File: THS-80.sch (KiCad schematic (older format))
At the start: 19 parts, among them J1 USB_B_Micro, J2 RC80 Bus, J3 RC80 Expansion, SW1 Reset, U1 MAX40203AUK, U2 DS1813R-5+T&R

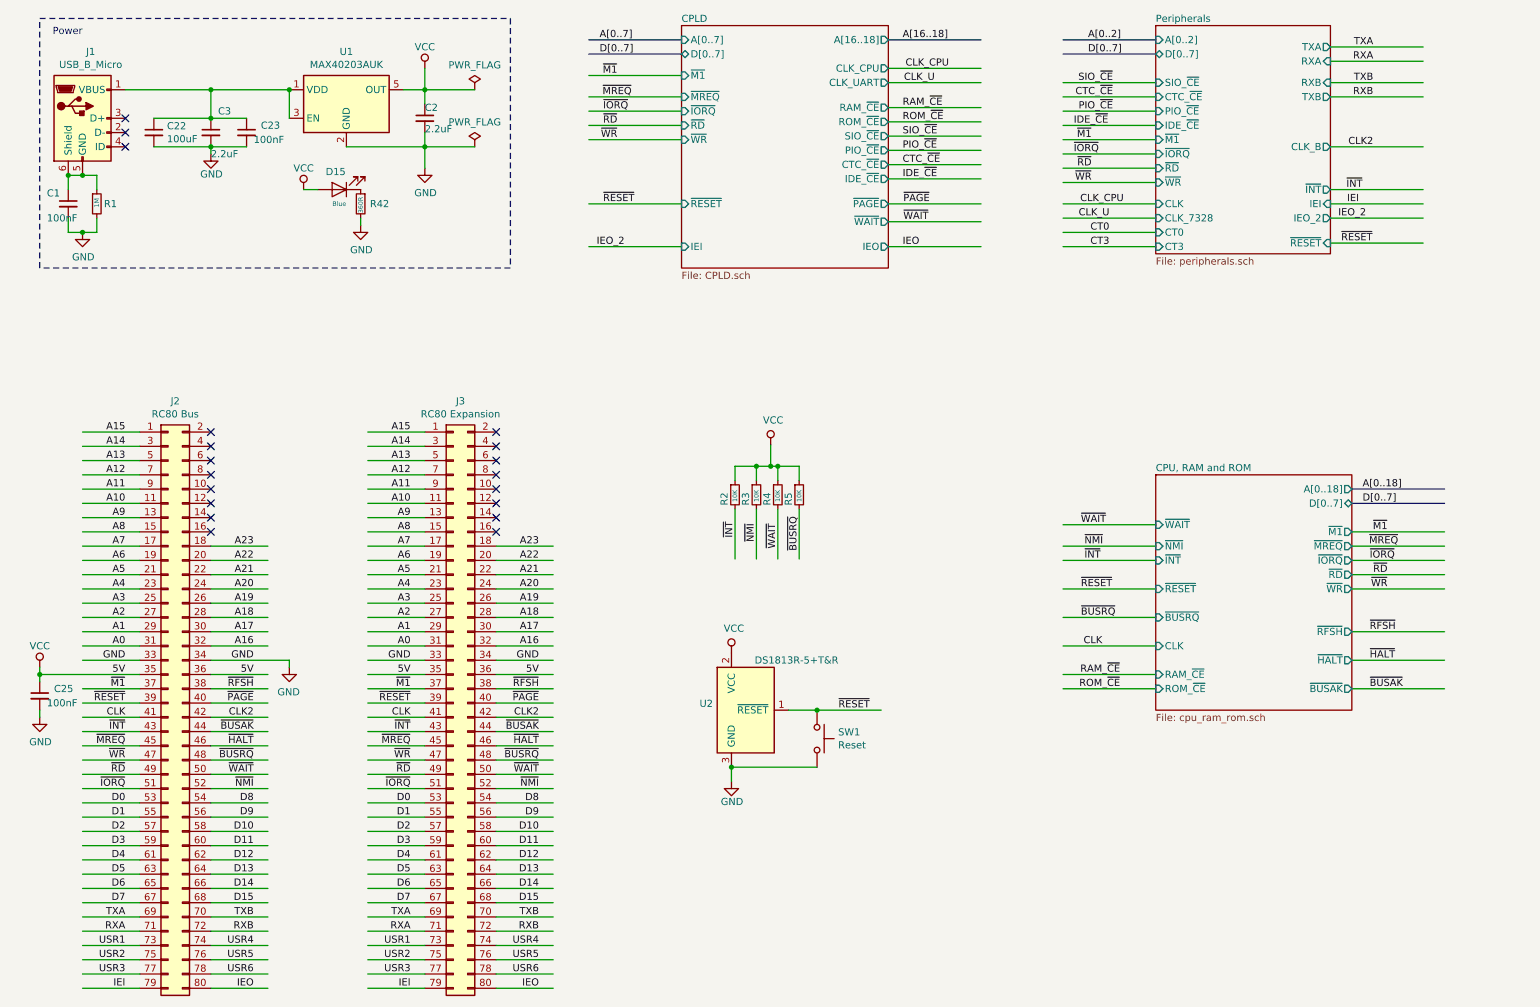
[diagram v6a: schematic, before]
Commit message: swapped CTC and PIO
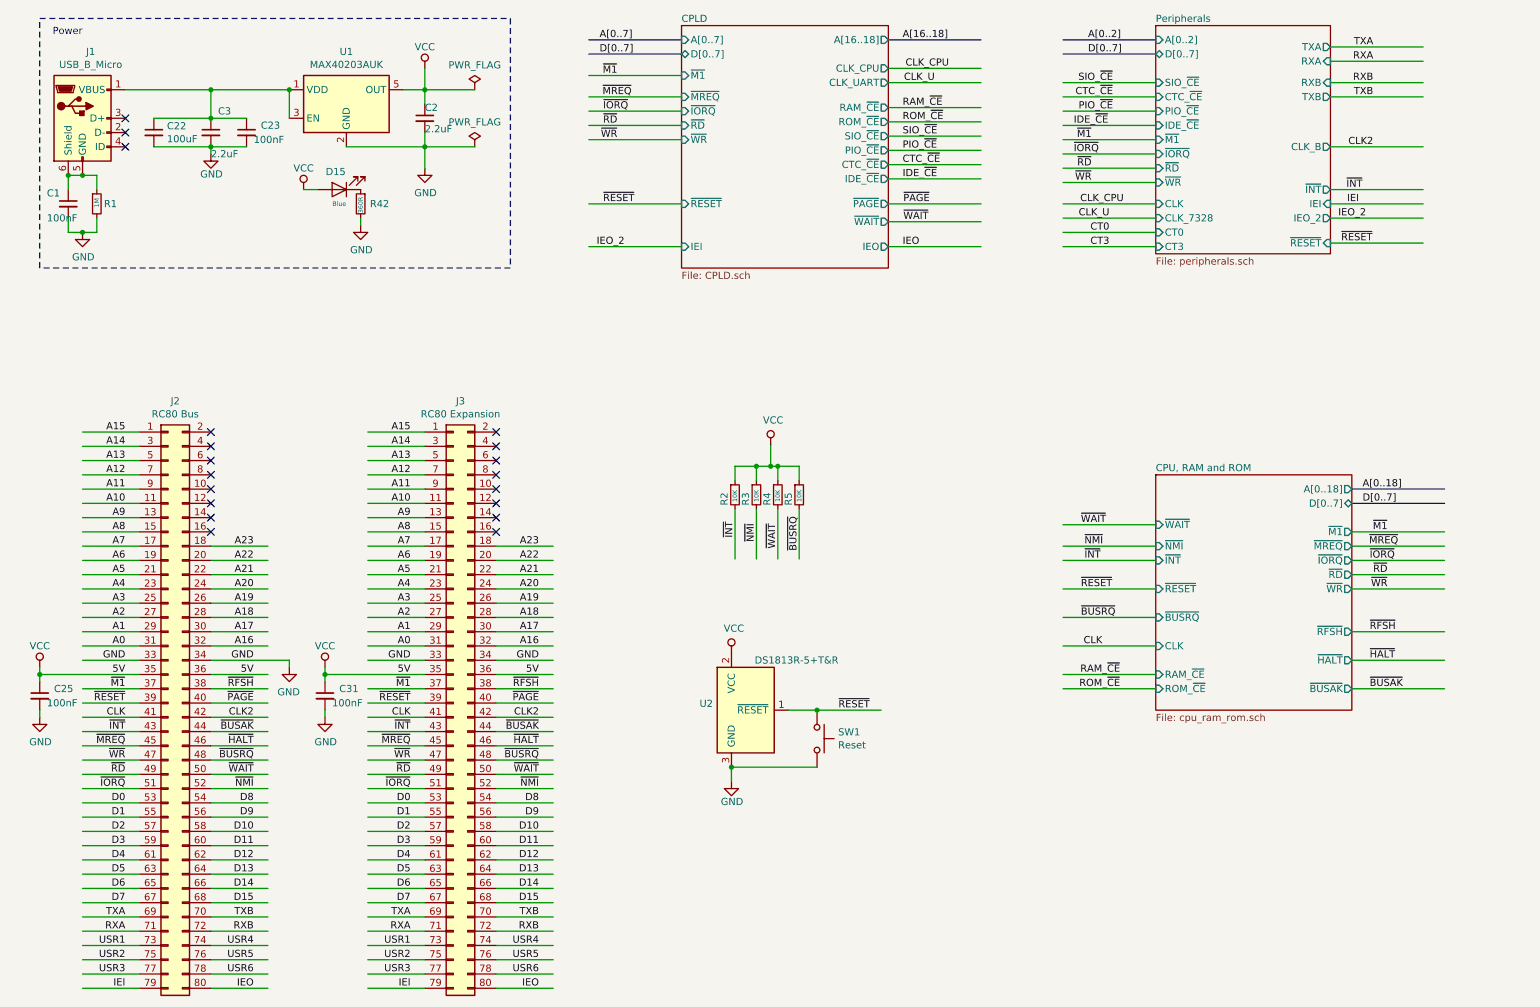
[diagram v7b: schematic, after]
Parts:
- added C31: 100nF, Capacitor_SMD:C_0603_1608Metric_Pad1.05x0.95mm_HandSolder, symbol Device:C_Small
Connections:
- wire segments 247 -> 250
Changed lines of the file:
@@
 Wire Wire Line
 	750  5350 750  5300
-Wire Wire Line
-	3450 5350 3050 5350
 $Comp
 L power:VCC #PWR05
@@
 RXA
 Wire Wire Line
+	9800 1300 10450 1300
+Wire Wire Line
 	9800 1200 10450 1200
-Wire Wire Line
-	9800 1300 10450 1300
+Text Label 10100 1300 2    50   ~ 0
+TXB
 Text Label 10100 1200 2    50   ~ 0
-TXB
-Text Label 10100 1300 2    50   ~ 0
 RXB
 $Sheet
@@
 Text Label 10100 1650 2    50   ~ 0
 CLK2
+Wire Wire Line
+	2750 5350 2750 5300
+$Comp
+L power:VCC #PWR0110
+U 1 1 5D9E4603
+P 2750 5300
+F 0 "#PWR0110" H 2750 5150 50  0001 C CNN
+F 1 "VCC" H 2750 5450 50  0000 C CNN
+F 2 "" H 2750 5300 50  0001 C CNN
+F 3 "" H 2750 5300 50  0001 C CNN
+	1    2750 5300
+	-1   0    0    -1
+$EndComp
+$Comp
+L Device:C_Small C31
+U 1 1 5D9E460E
+P 2750 5500
+F 0 "C31" H 2850 5550 50  0000 L CNN
+F 1 "100nF" H 2800 5450 50  0000 L CNN
+F 2 "Capacitor_SMD:C_0603_1608Metric_Pad1.05x0.95mm_HandSolder" H 2788 5350 50  0001 C CNN
+F 3 "https://www.mouser.com/datasheet/2/212/KEM_C1002_X7R_SMD-1102033.pdf" H 2750 5500 50  0001 C CNN
+F 4 "KEMET" H -3900 -1200 50  0001 C CNN "MFR"
+F 5 "C0805C105K4RACTU" H -3900 -1200 50  0001 C CNN "MPN"
+F 6 "Mouser" H -3900 -1200 50  0001 C CNN "SPR"
+F 7 "80-C0805C105K4R" H -3900 -1200 50  0001 C CNN "SPN"
+F 8 "https://www.mouser.com/ProductDetail/KEMET/C0805C105K8RAC7210?qs=sGAEpiMZZMs0AnBnWHyRQOf5HOpVaXbh6p7WVhSDTqQ%3D" H -3900 -1200 50  0001 C CNN "SPURL"
+	1    2750 5500
+	1    0    0    -1
+$EndComp
+Wire Wire Line
+	2750 5400 2750 5350
+Wire Wire Line
+	2750 5600 2750 5650
+$Comp
+L power:GND #PWR0111
+U 1 1 5D9E4616
+P 2750 5650
+AR Path="/5D9E4616" Ref="#PWR0111"  Part="1"
+AR Path="/5CB63856/5D9E4616" Ref="#PWR?"  Part="1"
+AR Path="/5CB5AB00/5CB63856/5D9E4616" Ref="#PWR?"  Part="1"
+F 0 "#PWR0111" H 2750 5400 50  0001 C CNN
+F 1 "GND" H 2755 5477 50  0000 C CNN
+F 2 "" H 2750 5650 50  0001 C CNN
+F 3 "" H 2750 5650 50  0001 C CNN
+	1    2750 5650
+	1    0    0    -1
+$EndComp
+Wire Wire Line
+	2750 5350 3450 5350
+Connection ~ 2750 5350
 $EndSCHEMATC

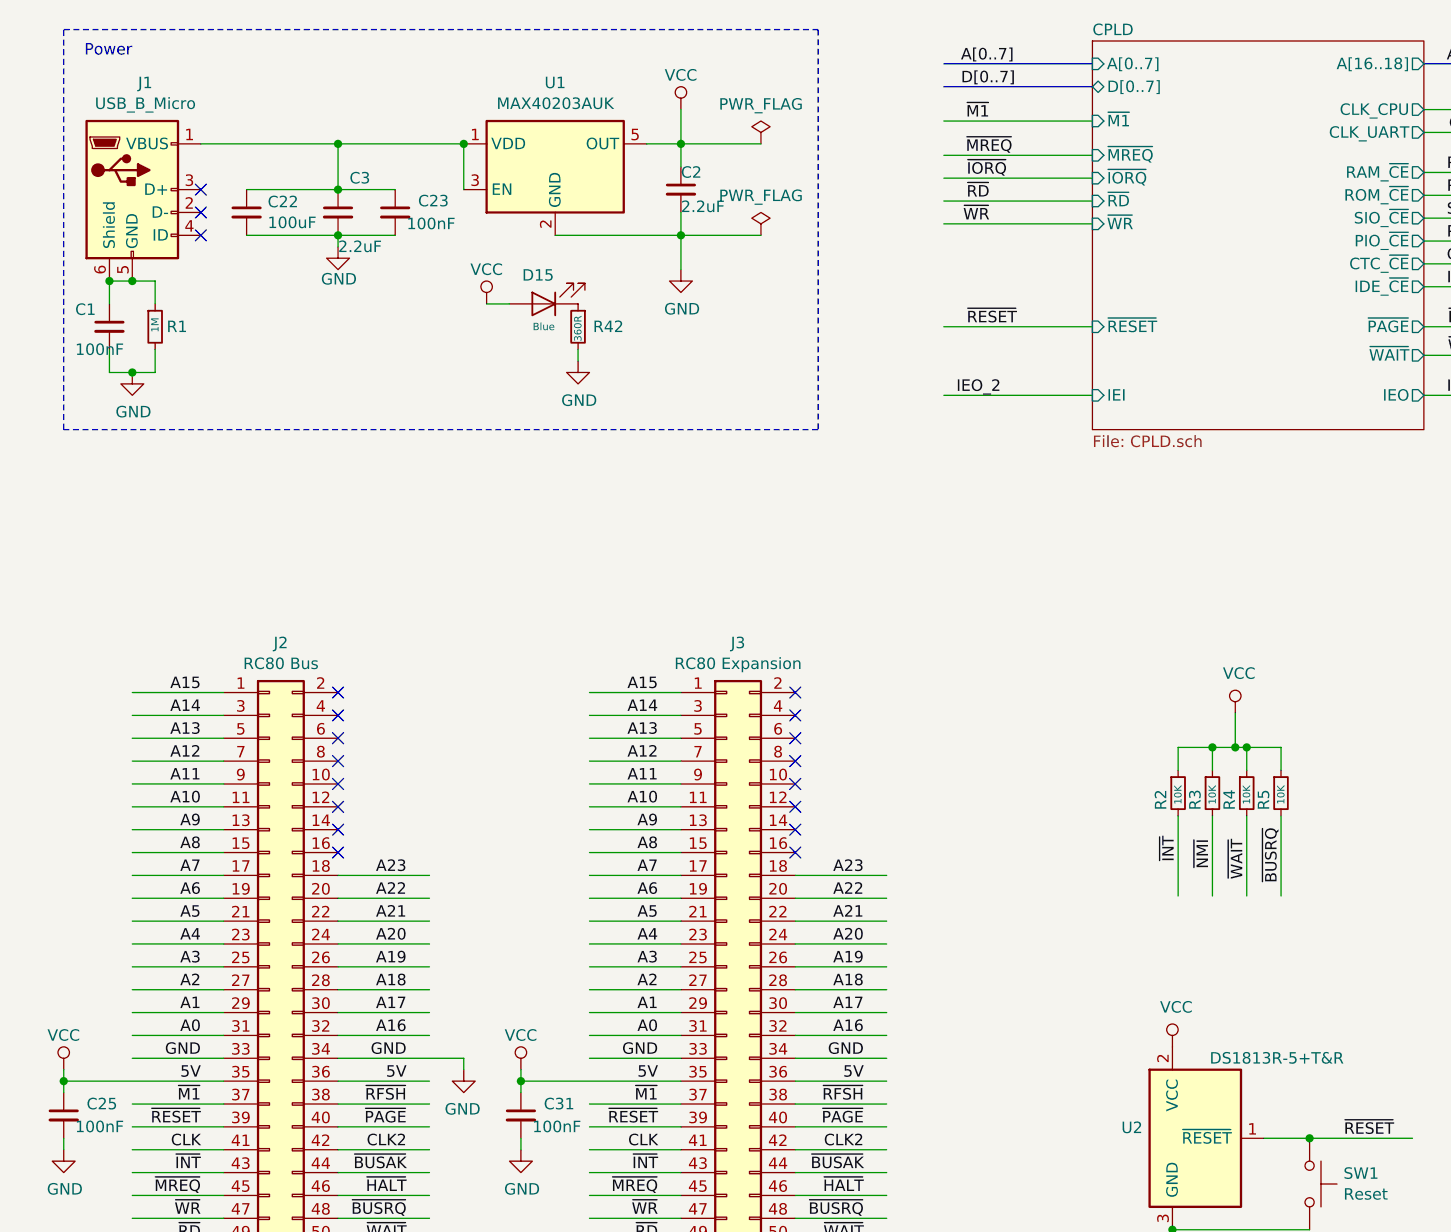
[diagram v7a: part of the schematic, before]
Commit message: replaced VCC with 5V, fixed ROM footprint
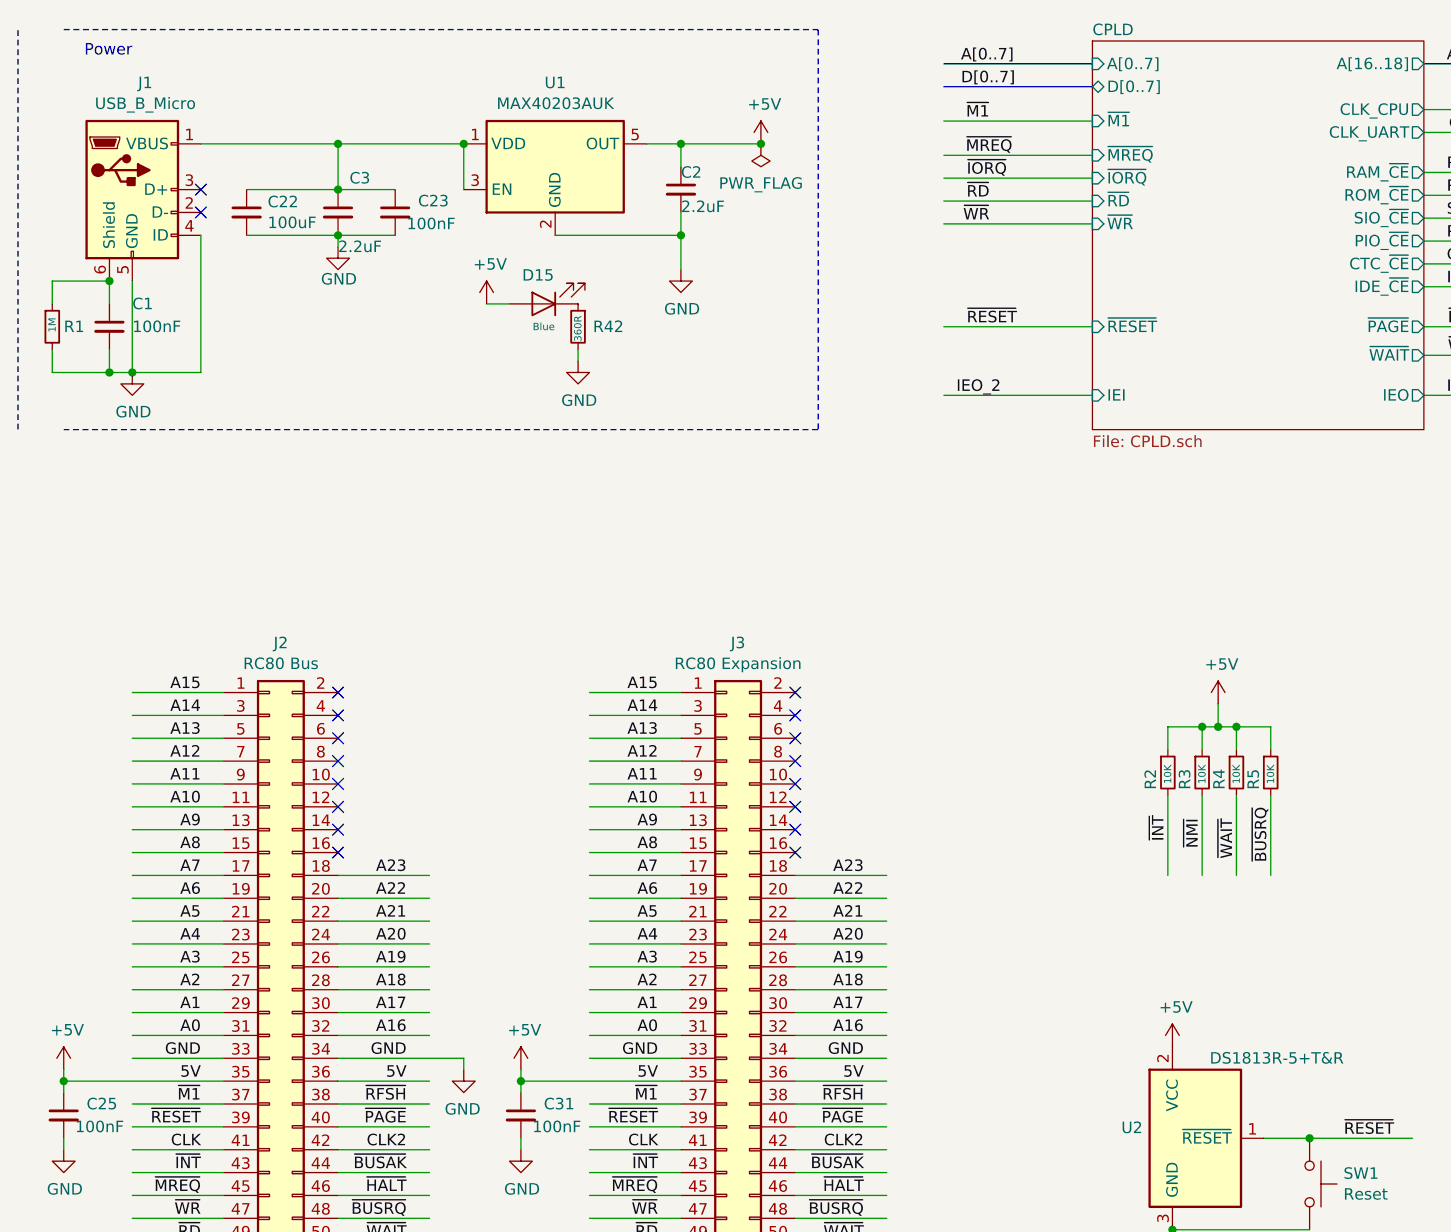
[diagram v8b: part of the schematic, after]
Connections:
- net labels added: +5V
- net labels removed: VCC
- no-connect marks 19 -> 18
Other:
- moved on the sheet: R1, R2, R3, R4, R5
